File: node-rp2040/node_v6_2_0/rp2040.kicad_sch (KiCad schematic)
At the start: 30 parts, among them SW2 PTS636 SM50J SMTR LFS, SW3 PTS636 SM50J SMTR LFS, U1 RP2040, U14 W25Q128, U2 USBLC6-2SC6, Y1 ABM8-272-T3

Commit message: finished layout v6.2
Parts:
- removed C8: 0.1u, JLCPCB:C_0402, symbol JLCPCB-Capacitors:0402,100nF
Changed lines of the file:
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@@
 	)
 	(junction
-		(at 104.14 25.4)
-		(diameter 0)
-		(color 0 0 0 0)
-	)
-	(junction
 		(at 71.12 78.74)
 		(diameter 0)
@@
 	)
 	(junction
-		(at 104.14 35.56)
-		(diameter 0)
-		(color 0 0 0 0)
-	)
-	(junction
 		(at 194.31 77.47)
 		(diameter 0)
@@
 	(wire
 		(pts
-			(xy 116.84 25.4) (xy 116.84 26.67)
-		)
-		(stroke
-			(width 0)
-			(type default)
-		)
-	)
-	(wire
-		(pts
 			(xy 104.14 34.29) (xy 104.14 35.56)
 		)
@@
 	(wire
 		(pts
-			(xy 116.84 34.29) (xy 116.84 35.56)
-		)
-		(stroke
-			(width 0)
-			(type default)
-		)
-	)
-	(wire
-		(pts
 			(xy 218.44 27.94) (xy 218.44 29.21)
 		)
@@
 	(wire
 		(pts
-			(xy 116.84 35.56) (xy 104.14 35.56)
-		)
-		(stroke
-			(width 0)
-			(type default)
-		)
-	)
-	(wire
-		(pts
 			(xy 179.07 113.03) (xy 179.07 114.3)
 		)
@@
 	(wire
 		(pts
-			(xy 104.14 25.4) (xy 116.84 25.4)
-		)
-		(stroke
-			(width 0)
-			(type default)
-		)
-	)
-	(wire
-		(pts
 			(xy 88.9 102.87) (xy 92.71 102.87)
 		)
@@
 					(unit 1)
 				)
-			)
-		)
-	)
-	(symbol
-		(lib_id "JLCPCB-Capacitors:0402,100nF")
-		(at 116.84 30.48 0)
-		(unit 1)
-		(exclude_from_sim no)
-		(in_bom yes)
-		(on_board yes)
-		(dnp no)
-		(fields_autoplaced yes)
-		(property "Reference" "C8"
-			(at 119.38 27.9399 0)
-			(effects
-				(font
-					(size 1.27 1.27)
-				)
-				(justify left)
-			)
-		)
-		(property "Value" "0.1u"
-			(at 119.38 30.4799 0)
-			(effects
-				(font
-					(size 1.27 1.27)
-				)
-				(justify left)
-			)
-		)
-		(property "Footprint" "JLCPCB:C_0402"
-			(at 115.062 30.48 90)
-			(effects
-				(font
-					(size 1.27 1.27)
-				)
-				(hide yes)
-			)
-		)
-		(property "Datasheet" "https://www.lcsc.com/datasheet/lcsc_datasheet_2304140030_Samsung-Electro-Mechanics-CL05B104KO5NNNC_C1525.pdf"
-			(at 116.84 30.48 0)
-			(effects
-				(font
-					(size 1.27 1.27)
-				)
-				(hide yes)
-			)
-		)
-		(property "Description" "16V 100nF X7R ±10% 0402 Multilayer Ceramic Capacitors MLCC - SMD/SMT ROHS"
-			(at 116.84 30.48 0)
-			(effects
-				(font
-					(size 1.27 1.27)
-				)
-				(hide yes)
-			)
-		)
-		(property "LCSC" "C1525"
-			(at 116.84 30.48 0)
-			(effects
-				(font
-					(size 1.27 1.27)
-				)
-				(hide yes)
-			)
-		)
-		(property "Stock" "10658398"
-			(at 116.84 30.48 0)
-			(effects
-				(font
-					(size 1.27 1.27)
-				)
-				(hide yes)
-			)
-		)
-		(property "Price" "0.004USD"
-			(at 116.84 30.48 0)
-			(effects
-				(font
-					(size 1.27 1.27)
-				)
-				(hide yes)
-			)
-		)
-		(property "Process" "SMT"
-			(at 116.84 30.48 0)
-			(effects
-				(font
-					(size 1.27 1.27)
-				)
-				(hide yes)
-			)
-		)
-		(property "Minimum Qty" "20"
-			(at 116.84 30.48 0)
-			(effects
-				(font
-					(size 1.27 1.27)
-				)
-				(hide yes)
-			)
-		)
-		(property "Attrition Qty" "10"
-			(at 116.84 30.48 0)
-			(effects
-				(font
-					(size 1.27 1.27)
-				)
-				(hide yes)
-			)
-		)
-		(property "Class" "Basic Component"
-			(at 116.84 30.48 0)
-			(effects
-				(font
-					(size 1.27 1.27)
-				)
-				(hide yes)
-			)
-		)
-		(property "Category" "Capacitors,Multilayer Ceramic Capacitors MLCC - SMD/SMT"
-			(at 116.84 30.48 0)
-			(effects
-				(font
-					(size 1.27 1.27)
-				)
-				(hide yes)
-			)
-		)
-		(property "Manufacturer" "Samsung Electro-Mechanics"
-			(at 116.84 30.48 0)
-			(effects
-				(font
-					(size 1.27 1.27)
-				)
-				(hide yes)
-			)
-		)
-		(property "Part" "CL05B104KO5NNNC"
-			(at 116.84 30.48 0)
-			(effects
-				(font
-					(size 1.27 1.27)
-				)
-				(hide yes)
-			)
-		)
-		(property "Voltage Rated" "16V"
-			(at 119.38 33.02 0)
-			(effects
-				(font
-					(size 0.8 0.8)
-				)
-				(justify left)
-			)
-		)
-		(property "Tolerance" "±10%"
-			(at 116.84 30.48 0)
-			(effects
-				(font
-					(size 1.27 1.27)
-				)
-				(hide yes)
-			)
-		)
-		(property "Capacitance" "100nF"
-			(at 116.84 30.48 0)
-			(effects
-				(font
-					(size 1.27 1.27)
-				)
-				(hide yes)
-			)
-		)
-		(property "Temperature Coefficient" "X7R"
-			(at 116.84 30.48 0)
-			(effects
-				(font
-					(size 1.27 1.27)
-				)
-				(hide yes)
-			)
-		)
-		(pin "2"
-		)
-		(pin "1"
-		)
-		(instances
-			(project "node_v4_0"
-				(path "/03dc898e-8f05-4377-b5c6-8a0f09836da8/97d6a4f8-0a43-4caa-bfdf-f6d51a8f6307"
-					(reference "C8")
-					(unit 1)
-				)

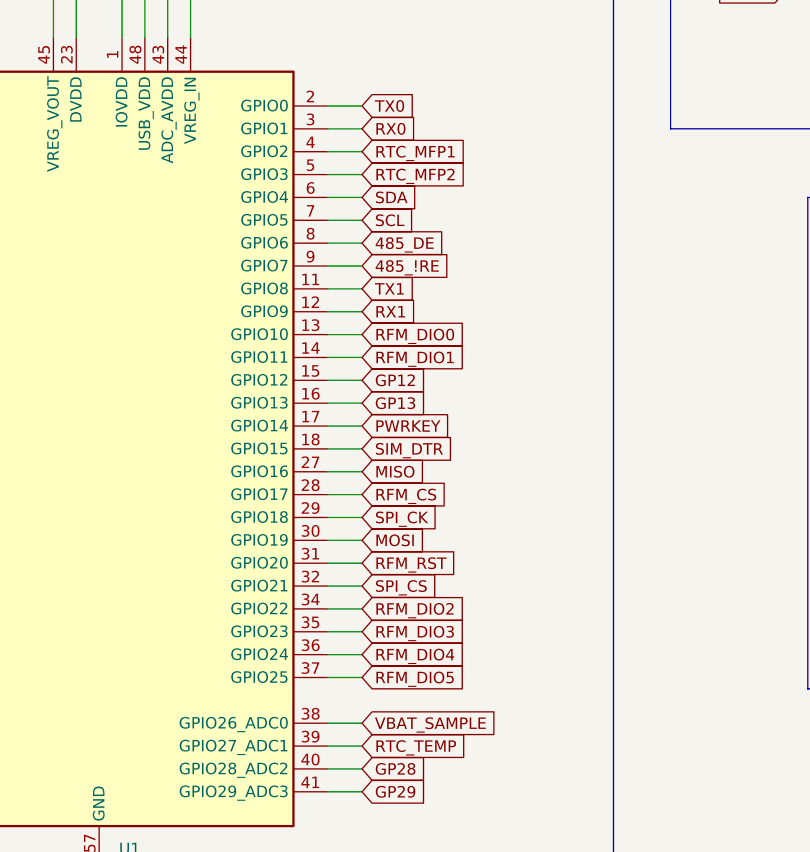
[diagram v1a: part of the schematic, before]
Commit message: finished routing; todo: labels and silkscreen, final review
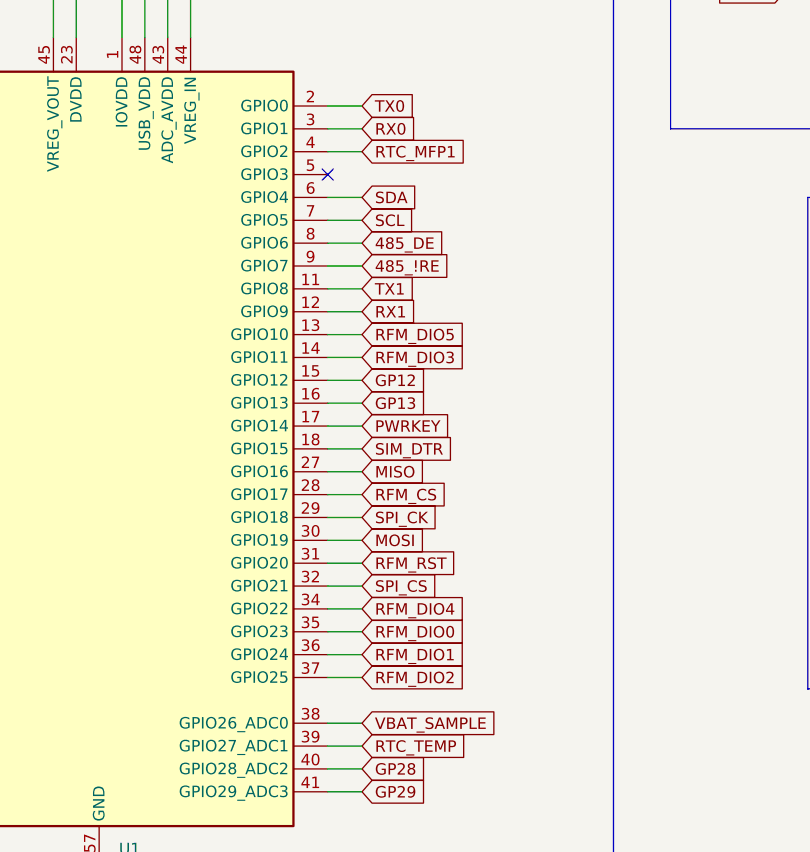
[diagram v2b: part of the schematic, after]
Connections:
- net RFM_DIO0: now also U1.35 (GPIO23); no longer U1.13 (GPIO10)
- net RFM_DIO1: now also U1.36 (GPIO24); no longer U1.14 (GPIO11)
- net RFM_DIO2: now also U1.37 (GPIO25); no longer U1.34 (GPIO22)
- net RFM_DIO3: now also U1.14 (GPIO11); no longer U1.35 (GPIO23)
- net RFM_DIO4: now also U1.34 (GPIO22); no longer U1.36 (GPIO24)
- net RFM_DIO5: now also U1.13 (GPIO10); no longer U1.37 (GPIO25)
- net RTC_MFP2: no longer names the net of U1.5 (GPIO3)
- no-connect marks 0 -> 1

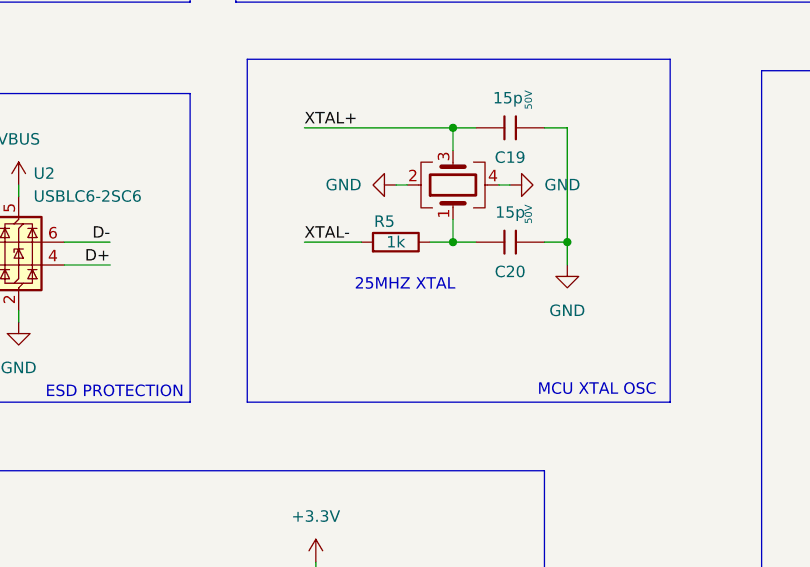
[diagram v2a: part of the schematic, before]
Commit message: added zener diode for overvoltage protection on vbus, small routing adjustments, silkscreen component labels
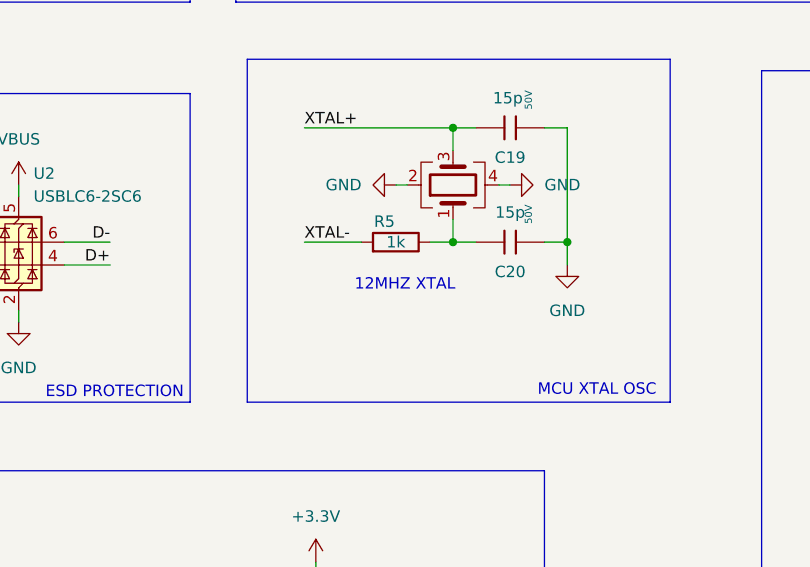
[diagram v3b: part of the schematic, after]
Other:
- note added: "12MHZ XTAL"
- note removed: "25MHZ XTAL"
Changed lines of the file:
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@@
 		)
 	)
-	(text "25MHZ XTAL"
+	(text "12MHZ XTAL"
 		(exclude_from_sim no)
 		(at 188.976 82.296 0)
